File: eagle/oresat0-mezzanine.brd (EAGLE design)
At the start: 80 x 71.5 mm, 29 parts, among them J1 R107064070, J10 R107064070, J2 R107064070, J3 R107064070, J4 R107064070, J5 R107064070, J6 R107064070, J7 R107064070, J8 R107064070, J9 R107064070, U1 QBA-07+, U2 QBA-07+, U3 QBA-07+, U7 QCN-19+, U8 QCN-19+, U9 QCN-19+

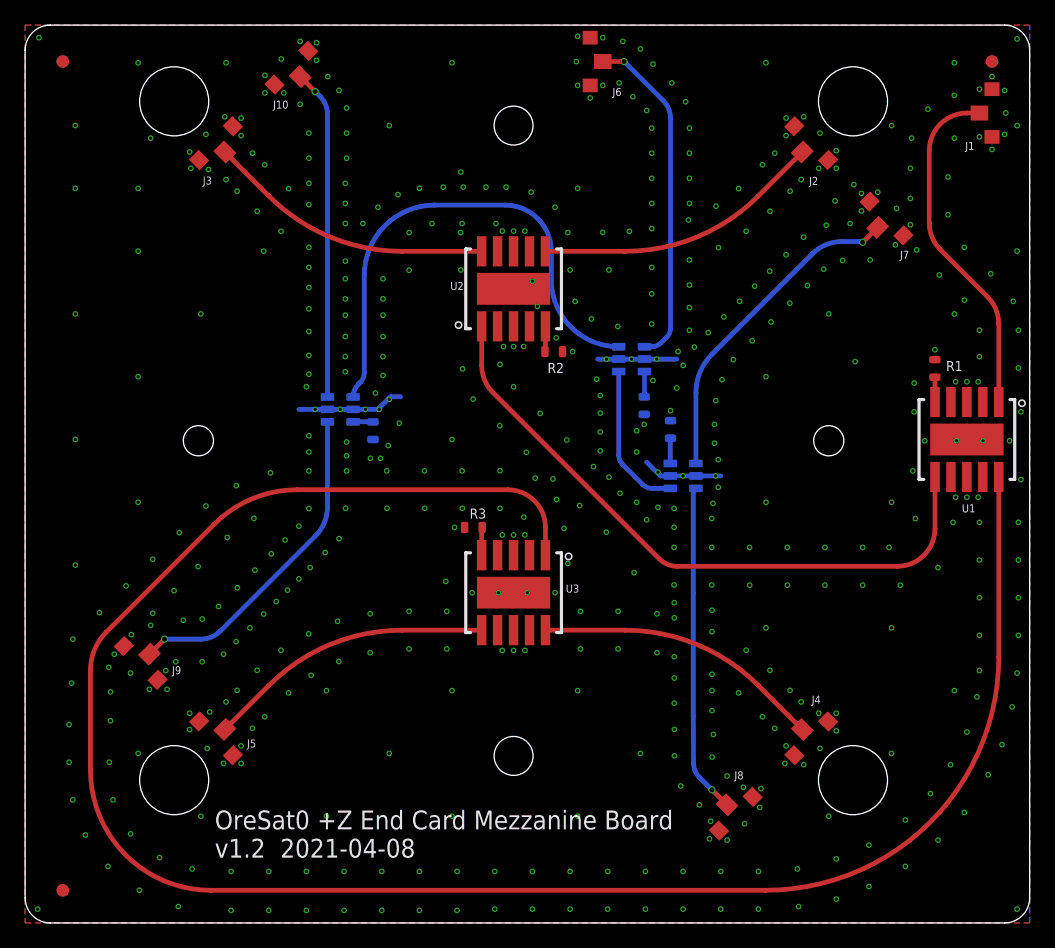
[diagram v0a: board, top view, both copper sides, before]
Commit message: v2.0 card, mezzanine, and BOM for v2.0. Moved UHF hybrids to avoid melt wire resistor leads. Updated BOM to reflect new v2.0 design.
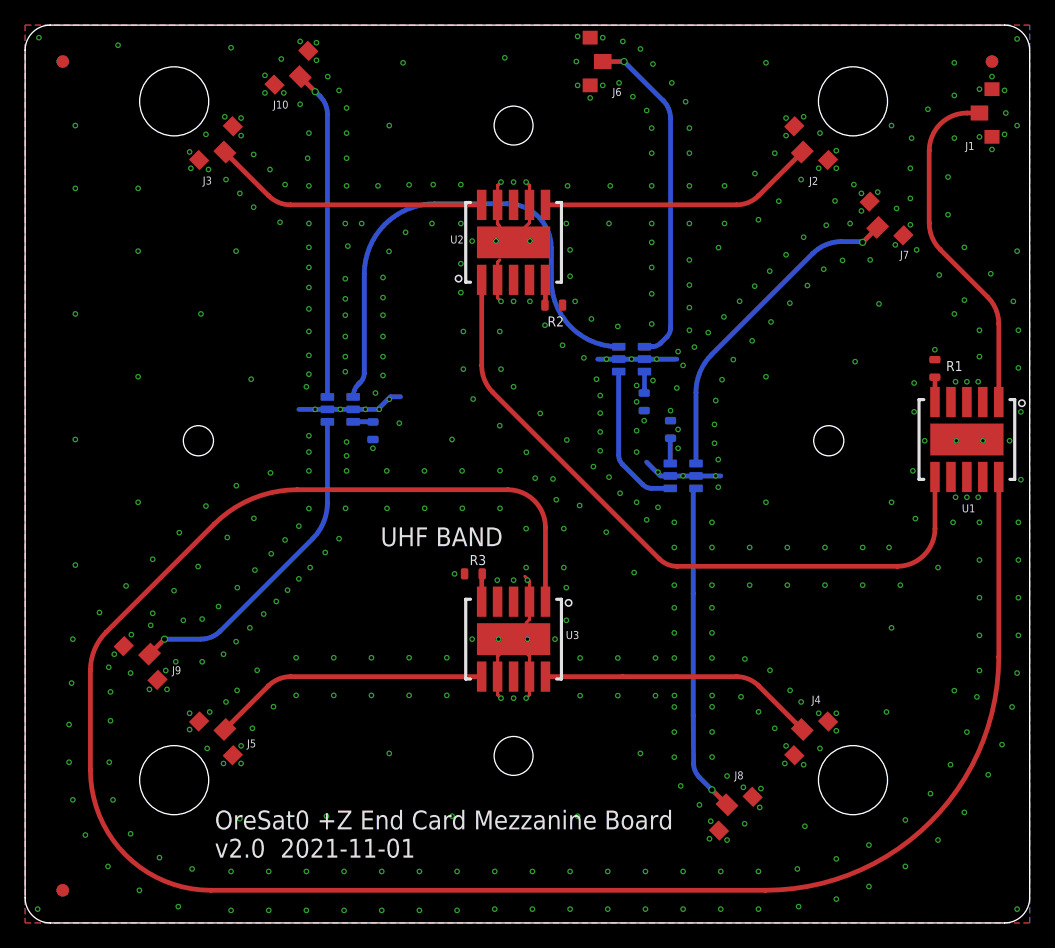
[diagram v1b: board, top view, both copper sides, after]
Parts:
- moved R2 3.70 mm to (53.1, 60.6)
- moved U3 3.70 mm to (49.9, 34.0)
- moved R3 3.70 mm to (46.7, 39.2)
- moved U2 3.70 mm to (49.9, 65.6)
- moved R4 0.30 mm to (60.3, 52.9)
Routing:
- net GND: track 21.3 -> 43.9 mm, vias 541 -> 531
- net UHF-SHORT: track 51.6 -> 55.3 mm
- net UHF-SHORT+1/4WAVE: track 152.1 -> 155.8 mm
- net UHF_270: track 22.8 -> 22.0 mm
- net UHF_180: track 22.8 -> 22.0 mm
- net UHF_0: track 22.8 -> 22.0 mm
- net UHF_90: track 22.8 -> 22.0 mm
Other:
- board text added: "L1 BAND"
- board text added: "OreSat0 +Z End Card Mezzanine Board v2.0 2021-11-01"
- board text added: "UHF BAND"
- board text removed: "OreSat0 +Z End Card Mezzanine Board v1.2 2021-04-08"
